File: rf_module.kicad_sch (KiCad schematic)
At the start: 32 parts, among them J10 HJ-SMA405, J9 1042240820, Q1 BC848, Q2 BC848, U4 SIM800C

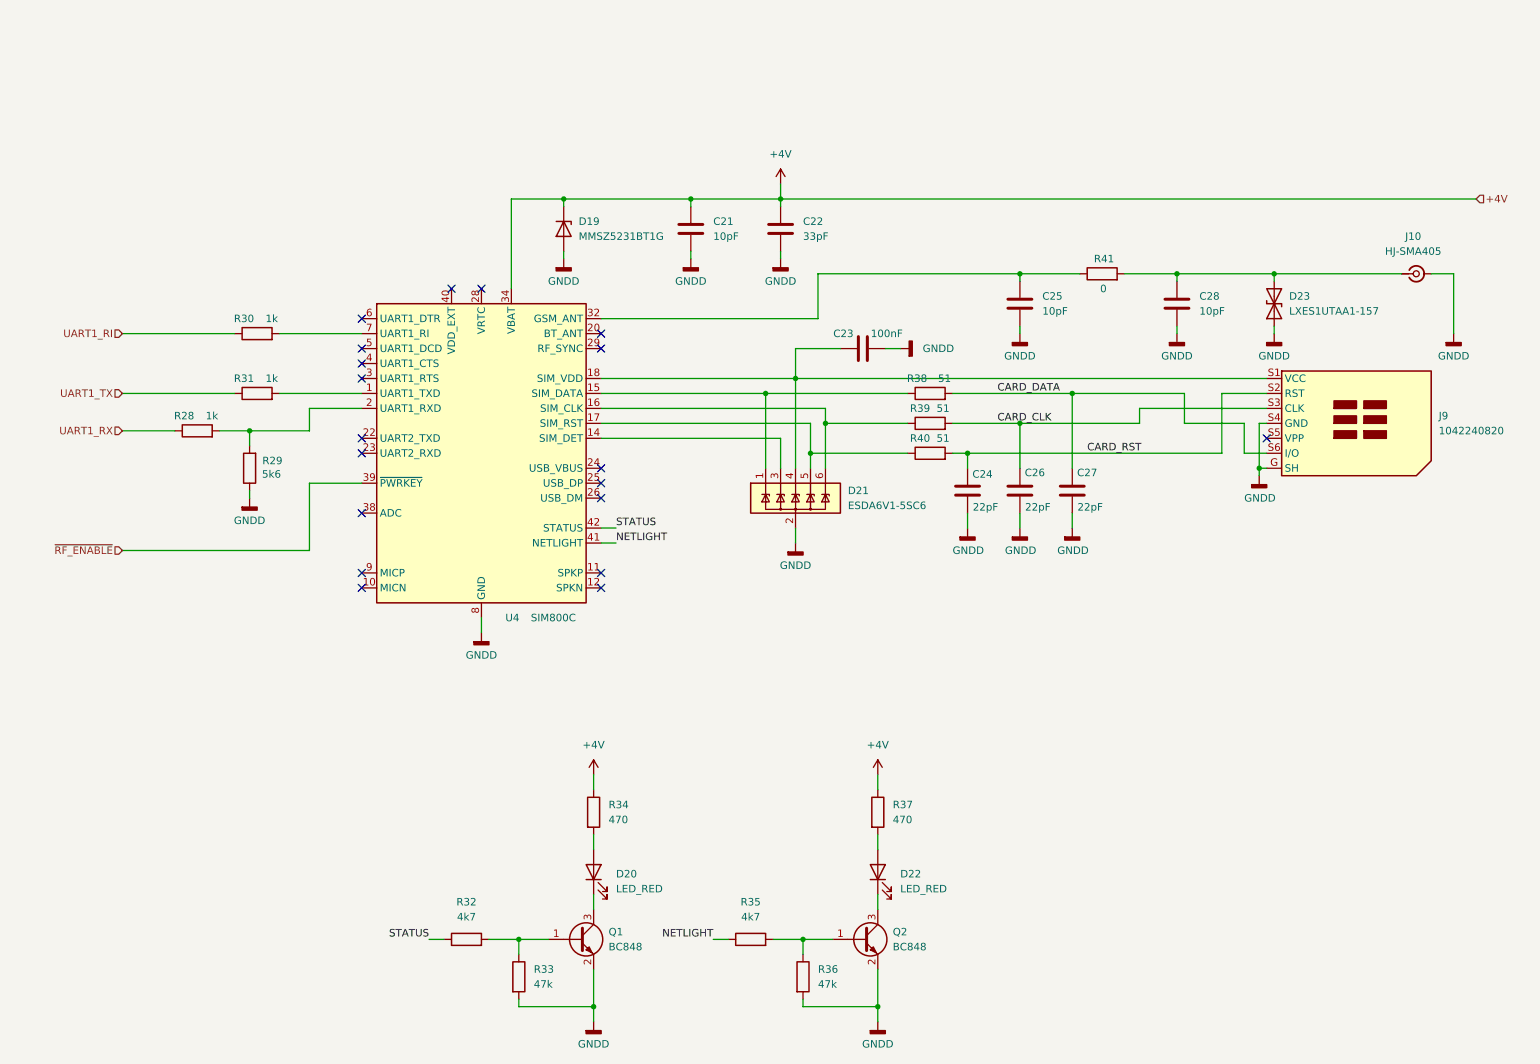
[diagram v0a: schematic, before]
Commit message: Dual SIM version
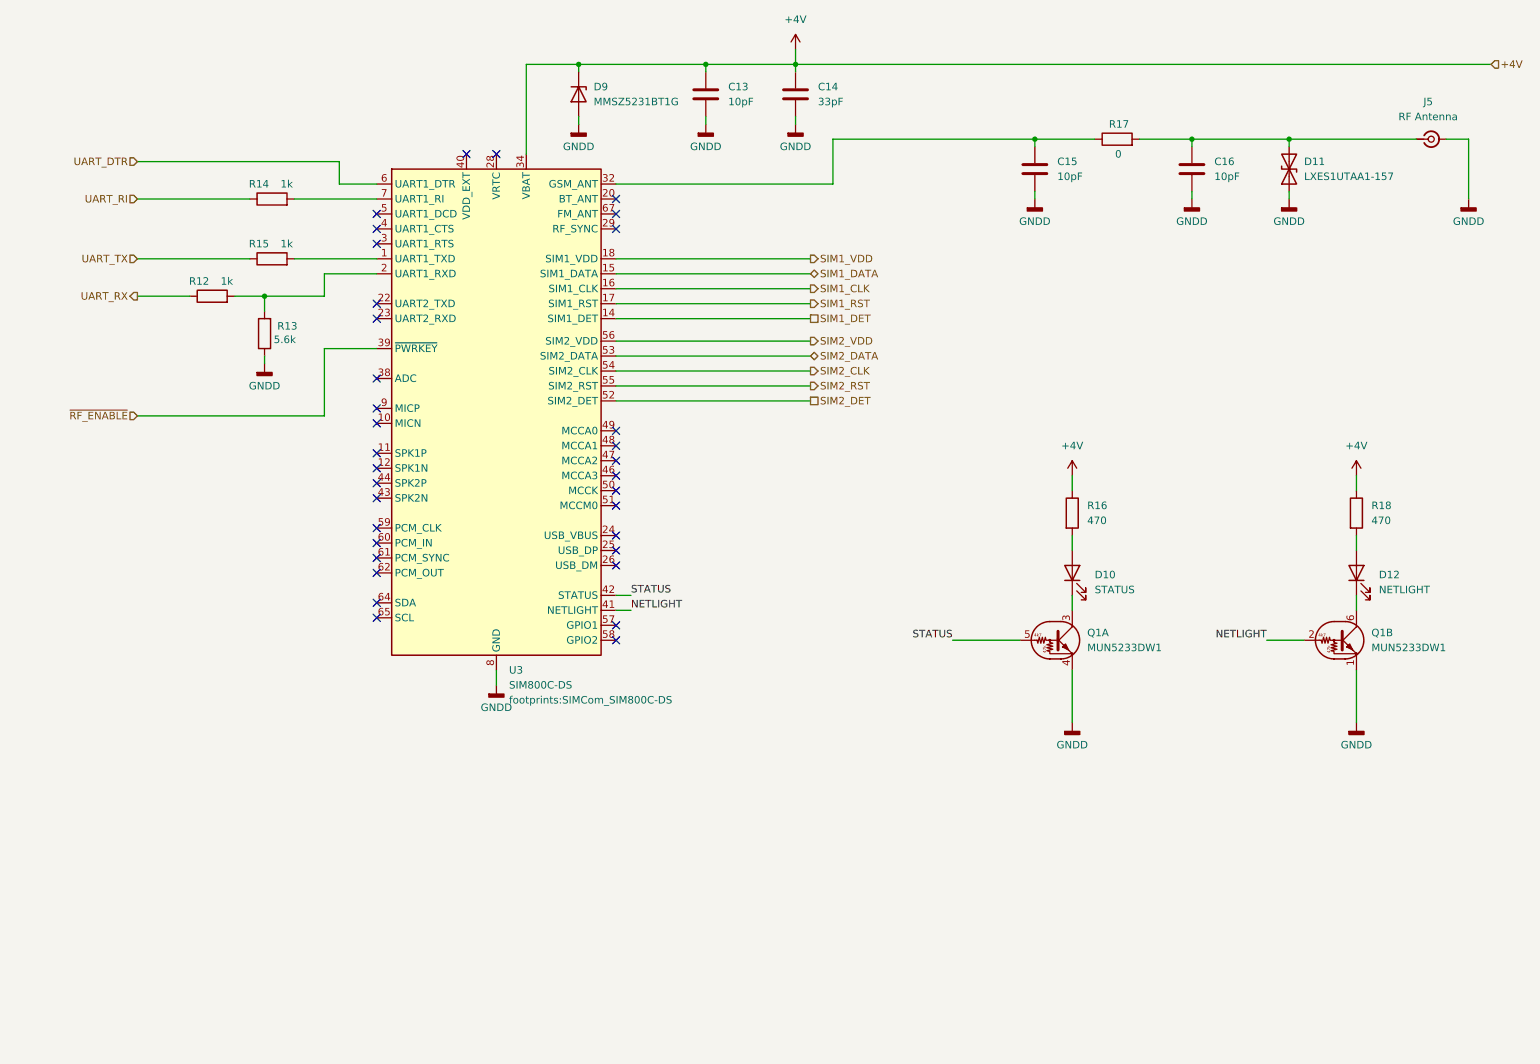
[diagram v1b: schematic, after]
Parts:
- removed C23: 100nF, Capacitor_SMD:C_0805_2012Metric_Pad1.18x1.45mm_HandSolder, symbol Device:C
- removed C24, C26, C27: 22pF, Capacitor_SMD:C_0805_2012Metric_Pad1.18x1.45mm_HandSolder, symbol Device:C
- removed D21: ESDA6V1-5SC6, Package_TO_SOT_SMD:SOT-23-6, symbol Power_Protection:ESDA6V1-5SC6
- removed J9: 1042240820, footprints:1042240820_MOLEX, symbol symbols:SIM_Card_Shielded_1042240820_Molex
- removed Q1, Q2: BC848, Package_TO_SOT_SMD:SOT-23, symbol Transistor_BJT:BC848
- removed R32, R35: 4k7, Resistor_SMD:R_0805_2012Metric_Pad1.20x1.40mm_HandSolder, symbol Device:R
- removed R33, R36: 47k, Resistor_SMD:R_0805_2012Metric_Pad1.20x1.40mm_HandSolder, symbol Device:R
- removed R38, R39, R40: 51, Resistor_SMD:R_0805_2012Metric_Pad1.20x1.40mm_HandSolder, symbol Device:R
- removed U4: SIM800C, RF_GSM:SIMCom_SIM800C, symbol RF_GSM:SIM800C
- added Q1: MUN5233DW1, Package_TO_SOT_SMD:SOT-363_SC-70-6, symbol symbols:MUN5233DW1
- added U3: SIM800C-DS, footprints:SIMCom_SIM800C-DS, symbol symbols:SIM800C-DS
- C13: renamed from C21; MPN (none) -> CC0805JRNPO9BN100; Manufacturer (none) -> YAGEO
- C14: renamed from C22; MPN (none) -> CC0805JRNPO9BN330; Manufacturer (none) -> YAGEO
- C15: renamed from C25; footprint Capacitor_SMD:C_0805_2012Metric_Pad1.18x1.45mm_HandSolder -> Capacitor_SMD:C_0603_1608Metric_Pad1.08x0.95mm_HandSolder; MPN (none) -> CC0603JRNPO9BN100; Manufacturer (none) -> YAGEO
- C16: renamed from C28; footprint Capacitor_SMD:C_0805_2012Metric_Pad1.18x1.45mm_HandSolder -> Capacitor_SMD:C_0603_1608Metric_Pad1.08x0.95mm_HandSolder; MPN (none) -> CC0603JRNPO9BN100; Manufacturer (none) -> YAGEO
- D10: renamed from D20; value LED_RED -> STATUS; MPN (none) -> FYLS-0805URC; Manufacturer (none) -> Ningbo Foryard Optoelectronics
- D11: renamed from D23; MPN (none) -> LXES1UTAA1-157; Manufacturer (none) -> Murata Electronics
- D12: renamed from D22; value LED_RED -> NETLIGHT; MPN (none) -> FYLS-0805URC; Manufacturer (none) -> Ningbo Foryard Optoelectronics
- D9: renamed from D19; MPN (none) -> MMSZ5231BT1G; Manufacturer (none) -> onsemi
- J5: renamed from J10; value HJ-SMA405 -> RF Antenna; MPN (none) -> HJ-SMA405; Manufacturer (none) -> Dongguan HJ Technology Co. Ltd
- R12: renamed from R28; MPN (none) -> RC0805JR-071KL; Manufacturer (none) -> YAGEO
- R13: renamed from R29; value 5k6 -> 5.6k; MPN (none) -> RC0805JR-075K6L; Manufacturer (none) -> YAGEO
- R14: renamed from R30; MPN (none) -> RC0805JR-071KL; Manufacturer (none) -> YAGEO
- R15: renamed from R31; MPN (none) -> RC0805JR-071KL; Manufacturer (none) -> YAGEO
- R16: renamed from R34; MPN (none) -> RC0805JR-07470RL; Manufacturer (none) -> YAGEO
- R17: renamed from R41; footprint Resistor_SMD:R_0805_2012Metric_Pad1.20x1.40mm_HandSolder -> Resistor_SMD:R_0603_1608Metric_Pad0.98x0.95mm_HandSolder; MPN (none) -> RC0603JR-070RL; Manufacturer (none) -> YAGEO
- R18: renamed from R37; MPN (none) -> RC0805JR-07470RL; Manufacturer (none) -> YAGEO
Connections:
- net +4V: now also U3.34 (VBAT), U3.35 (VBAT)
- net GNDD: now also Q1.1 (E), Q1.4 (E), U3.13 (GND), U3.19 (GND), U3.21 (GND), U3.27 (GND), U3.30 (GND), U3.31 (GND), U3.33 (GND), U3.36 (GND), U3.37 (GND), U3.45 (GND), U3.63 (GND), U3.66 (GND), U3.68 (GND), U3.69 (GND), U3.70 (GND), U3.71 (GND), U3.72 (GND), U3.73 (GND), U3.74 (GND), U3.75 (GND), U3.76 (GND), U3.77 (GND), U3.8 (GND)
- net NETLIGHT: now also Q1.2 (B), U3.41 (NETLIGHT)
- net STATUS: now also Q1.5 (B), U3.42 (STATUS)
- net ~{RF_ENABLE}: now also U3.39 (~{PWRKEY})
- net at R12.2, R13.2: now also U3.2 (UART1_RXD)
- net at D10.1 (K): now also Q1.3 (C)
- net at C15.2, R17.1: now also U3.32 (GSM_ANT)
- net at D12.1 (K): now also Q1.6 (C)
- net at R15.2: now also U3.1 (UART1_TXD)
- net at R14.2: now also U3.7 (UART1_RI)
- net UART1_RI renamed UART_RI
- net UART1_RX renamed UART_RX
- net UART1_TX renamed UART_TX
- new net SIM1_CLK: U3.16 (SIM1_CLK)
- new net SIM1_DATA: U3.15 (SIM1_DATA)
- new net SIM1_DET: U3.14 (SIM1_DET)
- new net SIM1_RST: U3.17 (SIM1_RST)
- new net SIM1_VDD: U3.18 (SIM1_VDD)
- new net SIM2_CLK: U3.54 (SIM2_CLK)
- new net SIM2_DATA: U3.53 (SIM2_DATA)
- new net SIM2_DET: U3.52 (SIM2_DET)
- new net SIM2_RST: U3.55 (SIM2_RST)
- new net SIM2_VDD: U3.56 (SIM2_VDD)
- new net UART_DTR: U3.6 (UART1_DTR)
- no-connect marks 19 -> 34
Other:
- moved on the sheet: C13, C14, C15, C16, D10, D11, D12, D9, J5, R12, R13, R14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

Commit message: Replace SIM800DC with A7682E
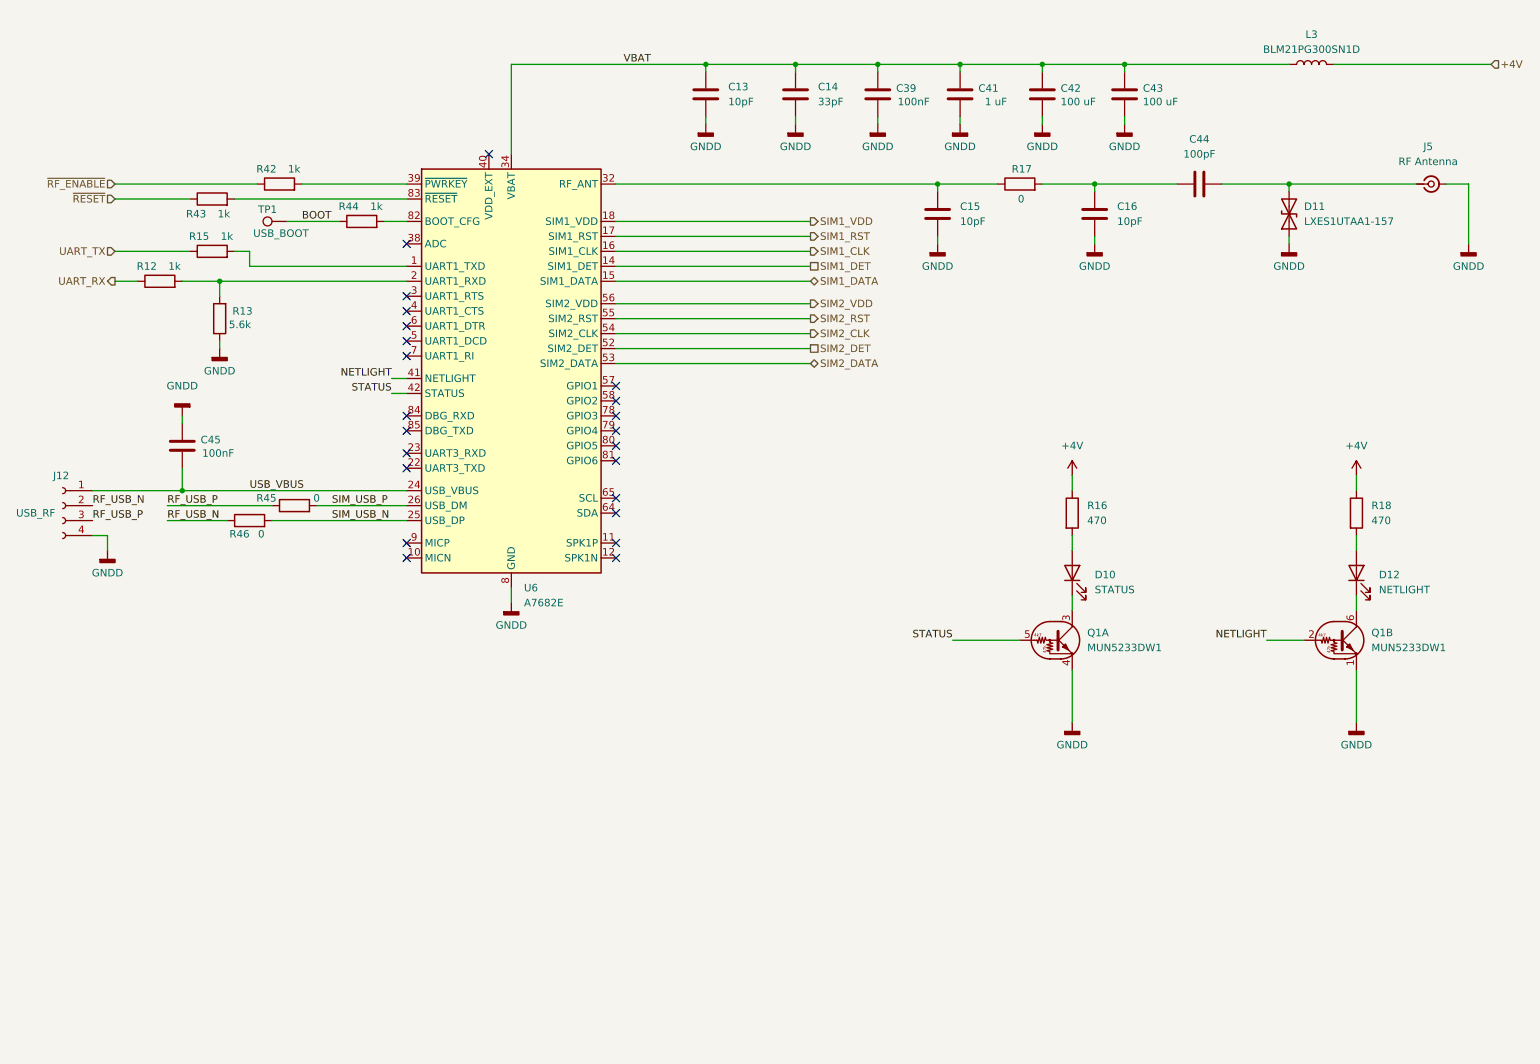
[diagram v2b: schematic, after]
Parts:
- removed D9: MMSZ5231BT1G, Diode_SMD:D_SOD-123, symbol Device:D_Zener
- removed R14: 1k, Resistor_SMD:R_0805_2012Metric_Pad1.20x1.40mm_HandSolder, symbol Device:R
- removed U3: SIM800C-DS, footprints:SIMCom_SIM800C-DS, symbol symbols:SIM800C-DS
- added C39, C45: 100nF, Capacitor_SMD:C_0805_2012Metric_Pad1.18x1.45mm_HandSolder, symbol Device:C
- added C41: 1 uF, Capacitor_SMD:C_0805_2012Metric_Pad1.18x1.45mm_HandSolder, symbol Device:C
- added C42, C43: 100 uF, Capacitor_SMD:C_1206_3216Metric_Pad1.33x1.80mm_HandSolder, symbol Device:C
- added C44: 100pF, Capacitor_SMD:C_0402_1005Metric, symbol Device:C
- added J12: USB_RF, Connector_PinHeader_1.27mm:PinHeader_1x04_P1.27mm_Vertical, symbol Connector:Conn_01x04_Socket
- added L3: BLM21PG300SN1D, Inductor_SMD:L_0805_2012Metric, symbol Device:L
- added R42, R43, R44: 1k, Resistor_SMD:R_0805_2012Metric_Pad1.20x1.40mm_HandSolder, symbol Device:R
- added R45, R46: 0, Resistor_SMD:R_0402_1005Metric, symbol Device:R
- added TP1: USB_BOOT, TestPoint:TestPoint_Pad_D2.0mm, symbol Connector:TestPoint
- added U6: A7682E, footprints:SIMCom_A7682E_LGA-85, symbol symbols:A7682E
- C15, C16: footprint Capacitor_SMD:C_0603_1608Metric_Pad1.08x0.95mm_HandSolder -> Capacitor_SMD:C_0402_1005Metric; MPN CC0603JRNPO9BN100 -> CC0402JRNPO9BN100
- D11: footprint Diode_SMD:D_01005_0402Metric_Pad0.57x0.30mm_HandSolder -> Diode_SMD:D_01005_0402Metric
- R17: footprint Resistor_SMD:R_0603_1608Metric_Pad0.98x0.95mm_HandSolder -> Resistor_SMD:R_0402_1005Metric; MPN RC0603JR-070RL -> RC0402JR-070RL
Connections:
- net +4V: now also L3.2; no longer C13.2, C14.2
- net GNDD: now also C39.1, C41.1, C42.1, C43.1, C45.2, J12.4 (Pin_4), U6.13 (GND), U6.19 (GND), U6.21 (GND), U6.27 (GND), U6.30 (GND), U6.31 (GND), U6.33 (GND), U6.36 (GND), U6.37 (GND), U6.45 (GND), U6.63 (GND), U6.66 (GND), U6.67 (GND), U6.69 (GND), U6.70 (GND), U6.71 (GND), U6.72 (GND), U6.73 (GND), U6.74 (GND), U6.75 (GND), U6.76 (GND), U6.77 (GND), U6.8 (GND)
- net NETLIGHT: now also U6.41 (NETLIGHT)
- net SIM1_CLK: now also U6.16 (SIM1_CLK)
- net SIM1_DATA: now also U6.15 (SIM1_DATA)
- net SIM1_DET: now also U6.14 (SIM1_DET)
- net SIM1_RST: now also U6.17 (SIM1_RST)
- net SIM1_VDD: now also U6.18 (SIM1_VDD)
- net SIM2_CLK: now also U6.54 (SIM2_CLK)
- net SIM2_DATA: now also U6.53 (SIM2_DATA)
- net SIM2_DET: now also U6.52 (SIM2_DET)
- net SIM2_RST: now also U6.55 (SIM2_RST)
- net SIM2_VDD: now also U6.56 (SIM2_VDD)
- net STATUS: now also U6.42 (STATUS)
- net ~{RF_ENABLE}: now also R42.1
- net at R12.2, R13.2: now also U6.2 (UART1_RXD)
- net at D11.2 (A2), J5.1 (In): now also C44.1; no longer C16.2, R17.2
- net at R15.2: now also U6.1 (UART1_TXD)
- net at C15.2, R17.1: now also U6.32 (RF_ANT)
- new net: U6.20 (NC), U6.28 (NC), U6.29 (NC), U6.43 (NC), U6.44 (NC), U6.46 (NC), U6.47 (NC), U6.48 (NC), U6.49 (NC), U6.50 (NC), U6.51 (NC), U6.59 (NC), U6.60 (NC), U6.61 (NC), U6.62 (NC), U6.68 (NC)
- new net: R42.2, U6.39 (~{PWRKEY})
- new net: R44.2, U6.82 (BOOT_CFG)
- new net: R43.2, U6.83 (~{RESET})
- new net: C16.2, C44.2, R17.2
- new net BOOT: R44.1, TP1.1
- new net RF_USB_N: J12.2 (Pin_2), R46.1
- new net RF_USB_P: J12.3 (Pin_3), R45.1
- new net SIM_USB_N: R46.2, U6.25 (USB_DP)
- new net SIM_USB_P: R45.2, U6.26 (USB_DM)
- new net USB_VBUS: C45.1, J12.1 (Pin_1), U6.24 (USB_VBUS)
- new net VBAT: C13.2, C14.2, C39.2, C41.2, C42.2, C43.2, L3.1, U6.34 (VBAT), U6.35 (VBAT)
- new net ~{RESET}: R43.1
- no-connect marks 34 -> 23
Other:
- moved on the sheet: C15, C16, D11, J5, R17
